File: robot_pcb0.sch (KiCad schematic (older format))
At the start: 0 parts

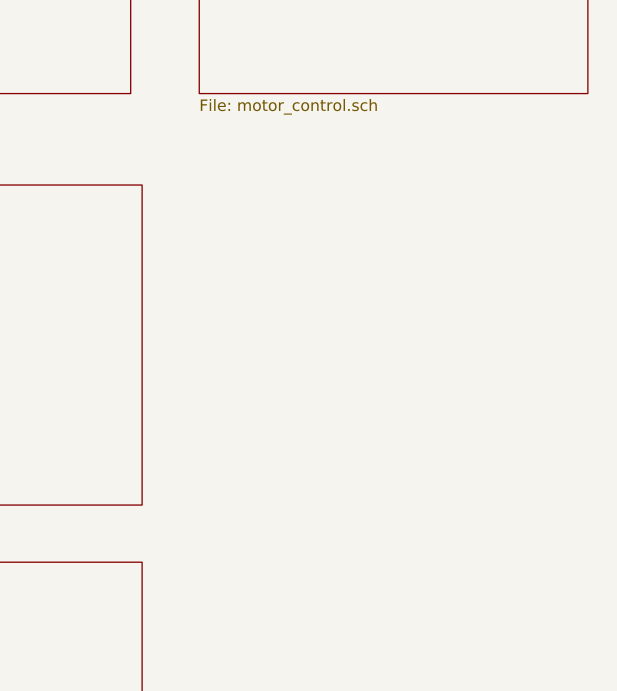
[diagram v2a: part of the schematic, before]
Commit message: adding an nrf52
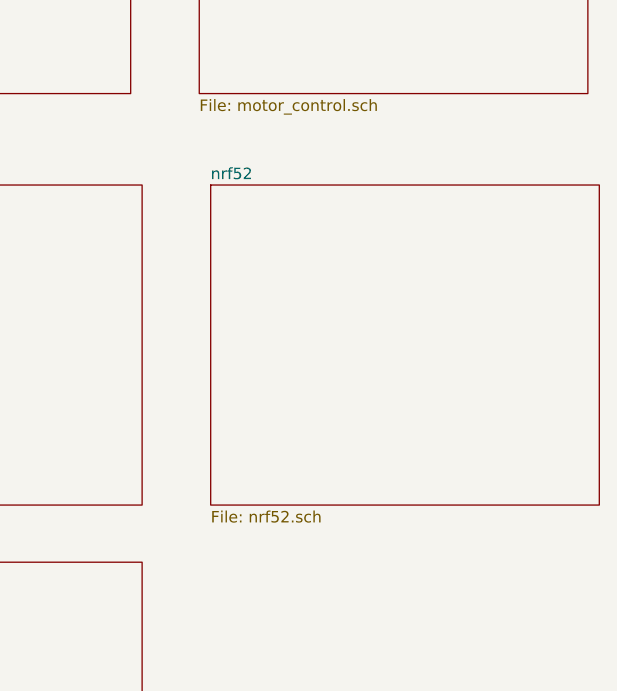
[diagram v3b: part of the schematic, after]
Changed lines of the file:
@@
 $Descr A4 11693 8268
 encoding utf-8
-Sheet 1 5
+Sheet 1 6
 Title "Four DC-Motor Controller"
 Date ""
@@
 Text Notes 3200 900  0    50   ~ 0
 DRV8833
+$Sheet
+S 2850 2450 1700 1400
+U 5CF66F52
+F0 "nrf52" 50
+F1 "nrf52.sch" 50
+$EndSheet
 $EndSCHEMATC
